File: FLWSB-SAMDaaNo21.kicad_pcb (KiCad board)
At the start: 2 copper layers, 51.4 x 18.5 mm, 36 parts, among them J1 USB4085-GF-A_REVA4, J2 DEBUG, J3 Conn_01x15_Male, J4 Conn_01x15_Male, SW1 SW_RESET, U1 LD1117S33TR_SOT223, U2 ATSAMD21G18A-A, Y1 Crystal_Small

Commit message: Laatste verbeteringen
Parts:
- removed D2, D3, D4, D5: D_Zener, Resistor_SMD:R_0805_2012Metric_Pad1.20x1.40mm_HandSolder
- added C13: 1µF, Capacitor_SMD:C_0805_2012Metric_Pad1.18x1.45mm_HandSolder, F.Cu at (134.6, 84.6)
- added J6: Conn_Coaxial, Connector_Coaxial:U.FL_Molex_MCRF_73412-0110_Vertical, F.Cu at (166.2, 78.7)
- added U3: RN2483, RN2483:RN2483, F.Cu at (149.1, 78.7)
- D1: value D_Zener -> PRTR5V0U2X; footprint Resistor_SMD:R_0805_2012Metric_Pad1.20x1.40mm_HandSolder -> Package_TO_SOT_SMD:SOT-143; moved to B.Cu
- SW1: footprint Button_Switch_SMD:SW_Push_1P1T_NO_6x6mm_H9.5mm -> KMR7_CNK:KMR7_CNK
- TP1, TP2, TP3: footprint TestPoint:TestPoint_Pad_D1.0mm -> TestPoint:TestPoint_THTPad_1.0x1.0mm_Drill0.5mm
- moved D1 6.08 mm to (85.6, 77.5), turned to 180 degrees
- moved TP2 1.59 mm to (97.8, 74.3)
- moved SW1 1.57 mm to (125.1, 78.7), turned to 90 degrees
- moved J3 1.27 mm to (96.5, 69.8)
- moved J4 1.27 mm to (132.1, 87.6)
- moved J1 0.84 mm to (85.7, 78.4)
- moved TP1 0.81 mm to (92.2, 82.3)
- moved C3 0.77 mm to (90.4, 84.6)
- moved R4 0.77 mm to (86.6, 84.6)
- moved R1 0.73 mm to (127.8, 76.2)
- moved C2 0.28 mm to (127.8, 81.3)
- renumbered C5 to locked
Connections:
- net PA09 renamed PA07
- net PA10 renamed RN2483_RESET
- D1 pad 1: VBUS -> GND
- D1 pad 2: Net-(C3-Pad2) -> USB-
- SW1 pad 1: Net-(R1-Pad1) -> unconnected-(SW1-Pad1)
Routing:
- net RN2483_RESET: track 14.9 -> 56.3 mm, vias 1 -> 2
- net VDDIN: track 95.0 -> 134.9 mm, vias 4 -> 3
- net SERCOM2_PAD1_TX: track 7.75 -> 35.9 mm, vias 0 -> 1
- net SERCOM2_PAD2_RX: track 10.1 -> 35.5 mm, vias 0 -> 1
- net GND: track 67.8 -> 80.1 mm, vias 11 -> 14
- net Net-(C3-Pad2): track 34.4 -> 22.9 mm
- net USB-: track 38.8 -> 30.2 mm
- net USB+: track 38.4 -> 32.3 mm
- net VBUS: track 22.0 -> 19.0 mm
- net 868MHz: track 0.00 -> 2.75 mm
- net VIN: track 14.7 -> 17.2 mm
- net SERCOM4_PAD0_SDA: track 19.7 -> 21.5 mm
- net PA20: track 5.36 -> 7.14 mm
- net PA19: track 6.62 -> 8.40 mm
- net PA21: track 5.79 -> 7.57 mm
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- added copper zone on In1.Cu, net GND
- added copper zone on In2.Cu, net VDDIN
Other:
- board size 51.4 x 18.5 mm -> 85.7 x 21 mm
- copper layers 2 -> 4
- board text added: "RESET SWDIO SWCLK"
- board text added: "V1 - 25/10/2022"

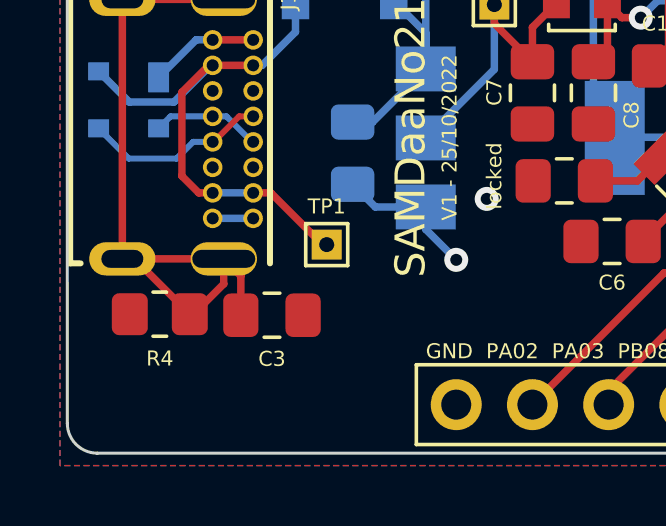
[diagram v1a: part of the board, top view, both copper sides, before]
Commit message: USB-C shell aan GND ipv R en C
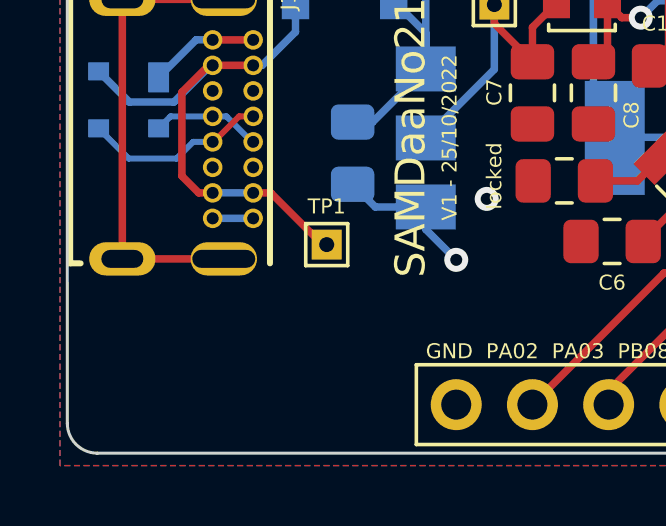
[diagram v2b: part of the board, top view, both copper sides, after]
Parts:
- removed C3: 4.5n, Capacitor_SMD:C_0805_2012Metric_Pad1.18x1.45mm_HandSolder
- removed R4: 1M, Resistor_SMD:R_0805_2012Metric_Pad1.20x1.40mm_HandSolder
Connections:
- J1 pad P1: Net-(C3-Pad2) -> GND
- J1 pad P2: Net-(C3-Pad2) -> GND
- J1 pad P3: Net-(C3-Pad2) -> GND
- J1 pad P4: Net-(C3-Pad2) -> GND
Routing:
- net Net-(C3-Pad2): track 22.9 -> 0.00 mm
- net GND: track 80.1 -> 95.9 mm
